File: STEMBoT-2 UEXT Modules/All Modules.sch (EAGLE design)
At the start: 132 parts, among them IC1 74HC165PW,118, IC2 74HC165PW,118, IC3 74HC165PW,118, J1 FTSH-105-01-XXX-DV-K, J2 FTSH-105-01-XXX-DV-K, J3 FTSH-105-01-XXX-DV-K, J4 FTSH-105-01-XXX-DV-K, J5 FTSH-105-01-XXX-DV-K, J6 FTSH-105-01-XXX-DV-K, Q1 MMBT3904LP-7, Q2 MMBT3904LP-7, Q3 MMBT3904LP-7, U1 TSL260R-LF, U10 SN74HC148D, U11 MAX964ESET, U12 MAX964ESET, U13 HC-SR04(NOSILK), U2 TESEO-LIV3F, U3 CYBLE-012011-00, U4 SN74HC148D, U5 MAX964ESET, U6 MAX964ESET, U7 SN74HC148D, U8 MAX964ESET, U9 MAX964ESET

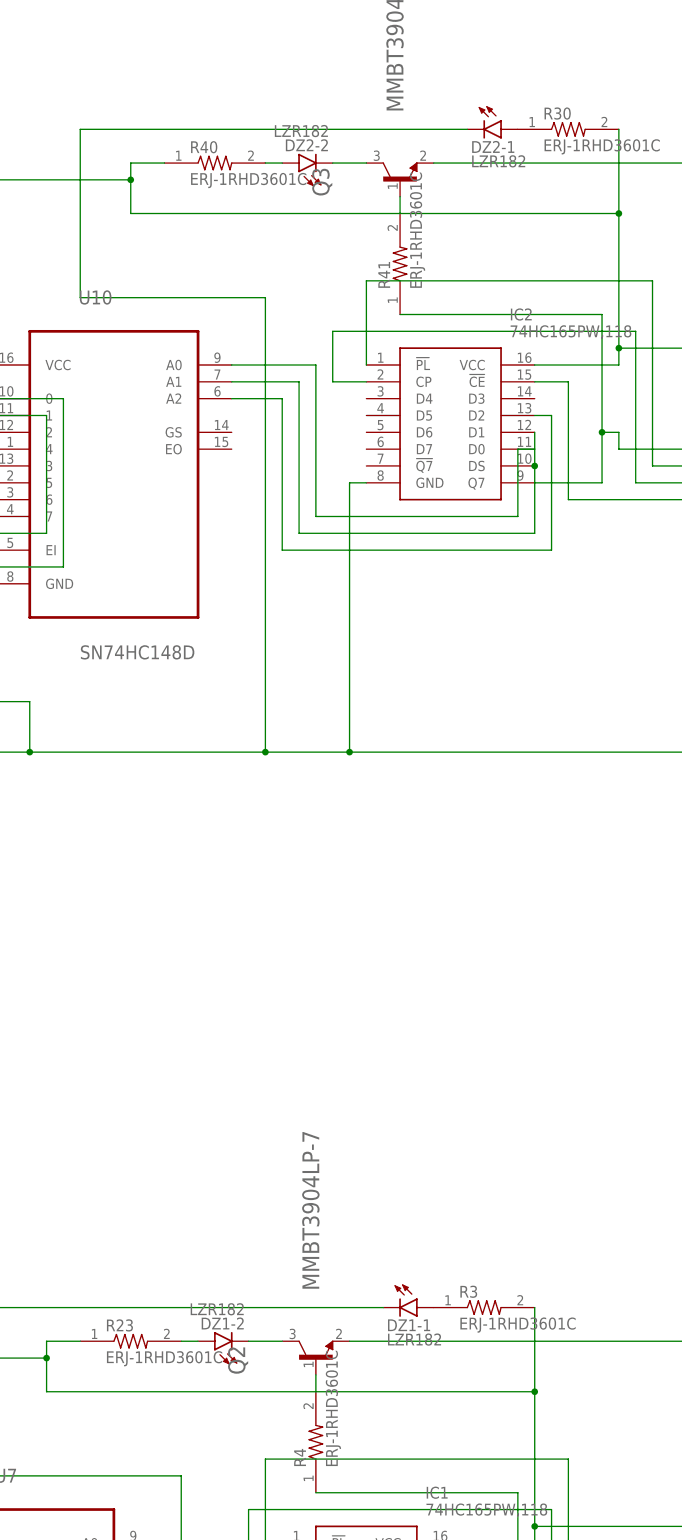
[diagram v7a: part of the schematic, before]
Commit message: update led footprint
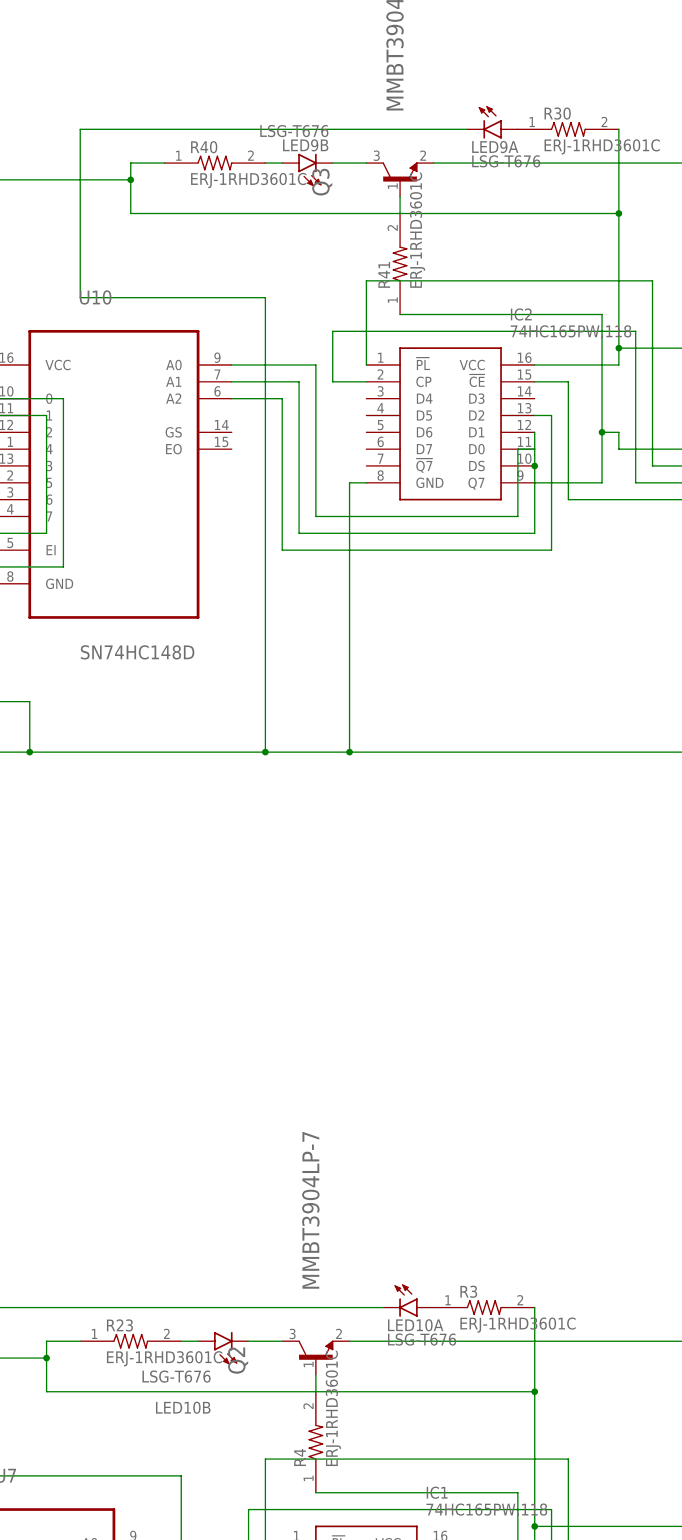
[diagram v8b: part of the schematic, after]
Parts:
- removed DZ1, DZ2: LZR182, led:LZR182
- added LED10, LED9: LSG-T676, led:LSG-T676
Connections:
- net N$10: now also LED10B.C; no longer DZ1-2.C
- net N$15: now also LED9B.C; no longer DZ2-2.C
- net N$18: now also LED10B.A; no longer DZ1-2.A
- net N$39: now also LED10A.C; no longer DZ1-1.C
- net N$5: now also LED9A.A; no longer DZ2-1.A
- net N$57: now also LED9B.A; no longer DZ2-2.A
- net N$64: now also LED9A.C; no longer DZ2-1.C
- net N$9: now also LED10A.A; no longer DZ1-1.A
